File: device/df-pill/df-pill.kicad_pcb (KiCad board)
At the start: 2 copper layers, 30 x 68.5 mm, 63 parts, among them J1 USB_B_Micro, P1 Connector_A, P2 Connector_B, P3 Connector_SWD, SW1 RESET, SW2 KEY, U1 MIC5219-3.3YM5, U2 STM32F103C8Tx, U3 USBLC6-2SC6, Y1 8MHz, Y2 32.768KHz

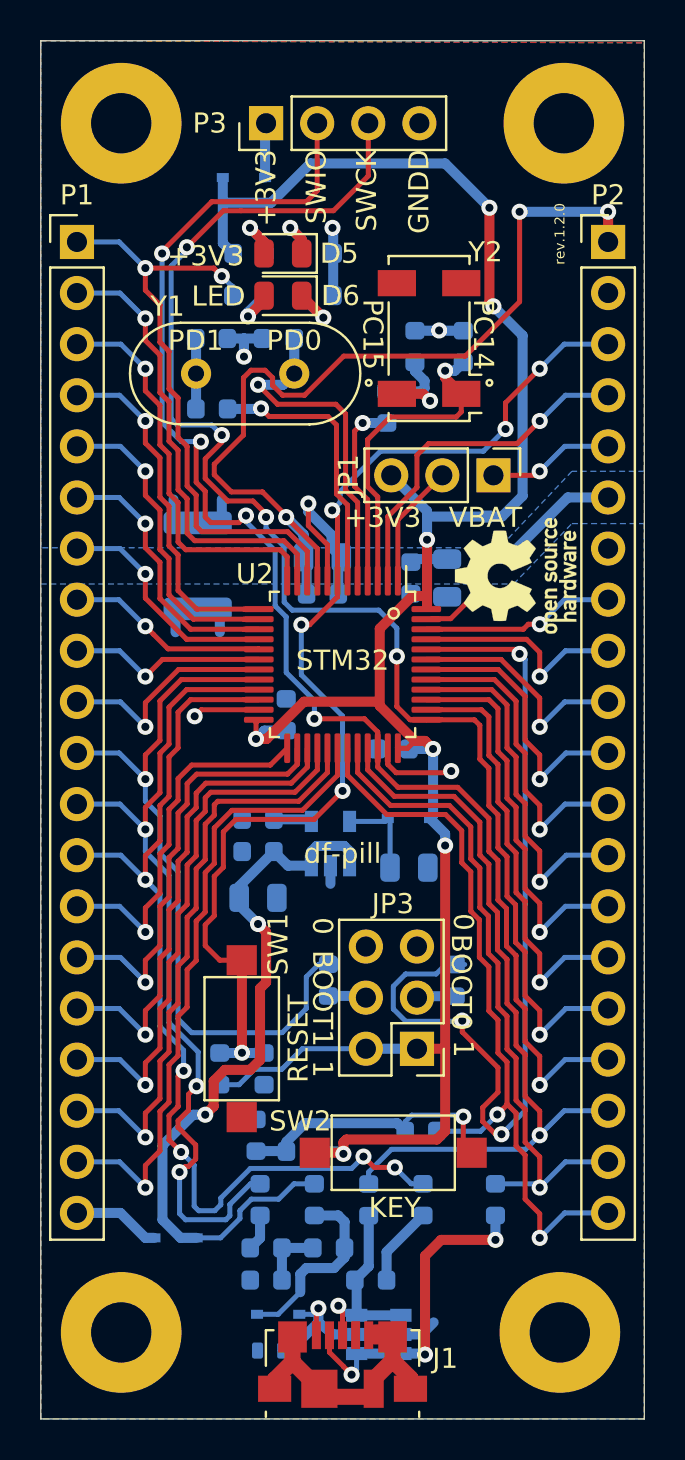
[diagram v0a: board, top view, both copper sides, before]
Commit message: rev.1.3.0
Fix schematic symbols and footprints to point to local library
Fix D4 position
Add R13 as a jumper for separating PC14 from LSE
Change Key from pull-down to pull-up
Remove C15 in favor of software debouncing for Key
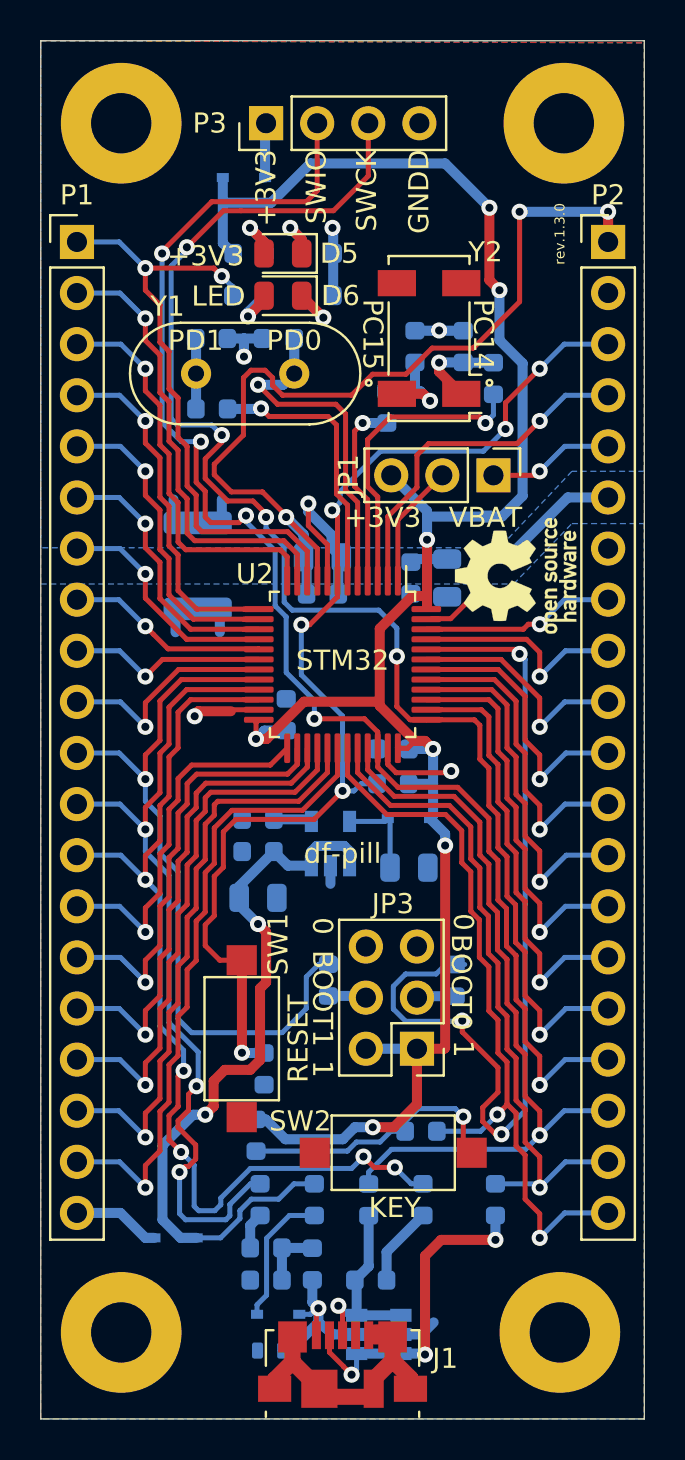
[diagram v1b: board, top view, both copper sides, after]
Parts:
- removed C15: 100nF, fp:C_0603_1608Metric
- added R13: 0, fp:R_0603_1608Metric, B.Cu at (153.8, 74.7)
- D7, D8: footprint Diode_SMD:D_SOD-323 -> fp:D_SOD-323
- moved R1 16.6 mm to (148.8, 94.8), turned to 180 degrees
- moved R6 1.14 mm to (144.8, 118.7), turned to 270 degrees
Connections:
- C14 pad 1: /PC14 -> Net-(C14-Pad1)
- R1 pad 1: /RESET -> VDD
- R1 pad 2: VDD -> /RESET
- R4 pad 2: GNDD -> VDD
- R6 pad 2: Net-(D4-Pad1) -> Net-(D2-Pad1)
- SW2 pad 1: VDD -> GNDD
- Y2 pad 1: /PC14 -> Net-(C14-Pad1)
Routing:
- net VDD: track 111.8 -> 103.8 mm
- net Net-(C14-Pad1): track 0.00 -> 4.72 mm, vias 0 -> 1
- net Net-(D4-Pad1): track 9.45 -> 6.82 mm
- net Net-(D2-Pad1): track 7.49 -> 9.03 mm
- net /RESET: track 55.9 -> 56.6 mm
- net /PC14: track 15.9 -> 15.3 mm
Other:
- board text added: "rev.1.3.0"
- board text removed: "rev.1.2.0"

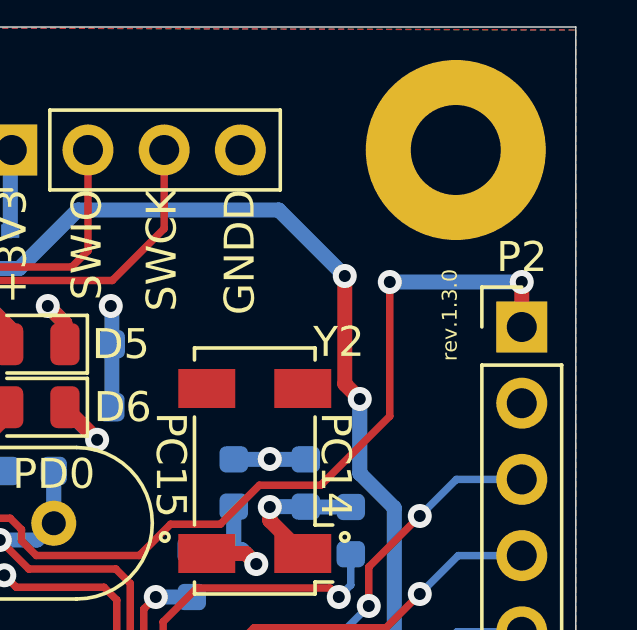
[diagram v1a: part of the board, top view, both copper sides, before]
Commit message: Fix silk layer for D1 and R1
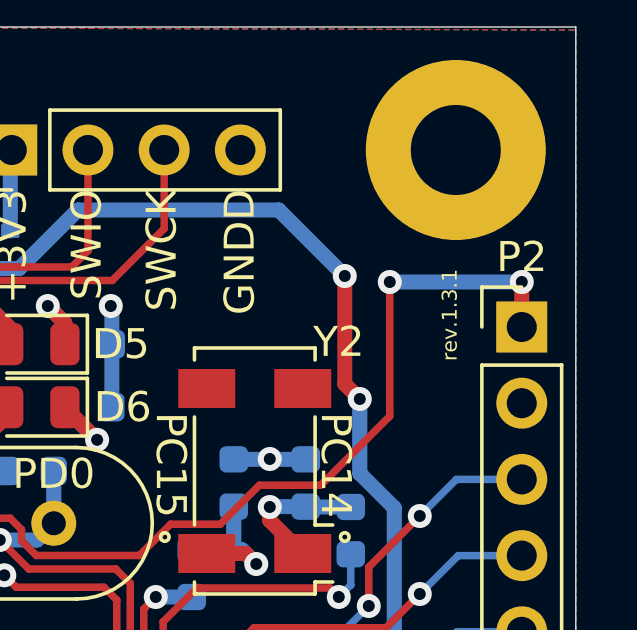
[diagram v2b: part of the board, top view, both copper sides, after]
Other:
- board text added: "rev.1.3.1"
- board text removed: "rev.1.3.0"
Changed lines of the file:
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@@
   (title_block
     (title df-pill)
-    (date 2020-06-22)
-    (rev 1.3.0)
+    (date 2021-01-08)
+    (rev 1.3.1)
     (company "by epchain")
     (comment 1 "Bluepill-like board with enhanced capabilities")
@@
     (34 B.Paste user)
     (35 F.Paste user)
-    (36 B.SilkS user hide)
-    (37 F.SilkS user hide)
+    (36 B.SilkS user)
+    (37 F.SilkS user)
     (38 B.Mask user)
     (39 F.Mask user)
@@
     (tags resistor)
     (attr smd)
-    (fp_text reference R1 (at 0 1.43) (layer B.SilkS)
+    (fp_text reference R1 (at -2.06 0.18 90) (layer B.SilkS)
       (effects (font (size 1 1) (thickness 0.15)) (justify mirror))
     )
@@
     (tags SOD-323)
     (attr smd)
-    (fp_text reference D1 (at 1.3 1.562) (layer B.SilkS)
+    (fp_text reference D1 (at -2.5 0.012) (layer B.SilkS)
       (effects (font (size 1 1) (thickness 0.15)) (justify mirror))
     )
@@
     (effects (font (size 0.5 0.5) (thickness 0.125)) (justify mirror))
   )
-  (gr_text rev.1.3.0 (at 157.1 67.5 90) (layer F.SilkS)
+  (gr_text rev.1.3.1 (at 157.1 67.5 90) (layer F.SilkS)
     (effects (font (size 0.5 0.5) (thickness 0.125)))
   )
